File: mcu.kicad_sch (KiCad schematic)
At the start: 46 parts, among them J1 10118193-0001LF, J5 Conn_ARM_SWD_TagConnect_TC2030, SW1 SW_Push, SW2 SW_Push, SW3 SW_Push, U1 RP2040, U2 AP2112K-3.3TRG1, U3 W25Q16JVSSIQ, Y3 12MHZ

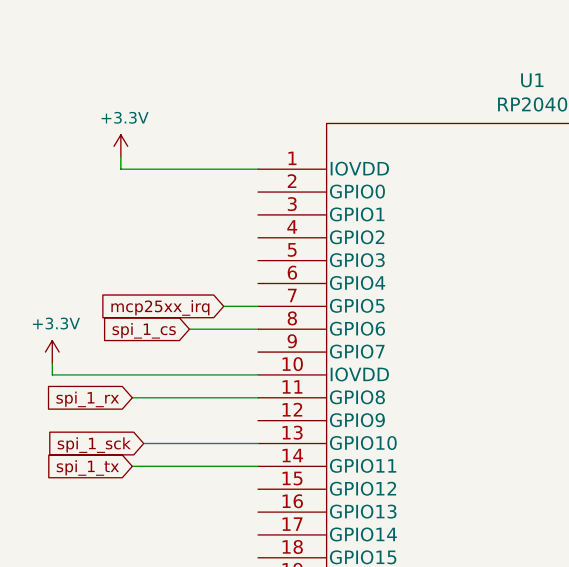
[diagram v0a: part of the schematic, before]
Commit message: move to 4 layers
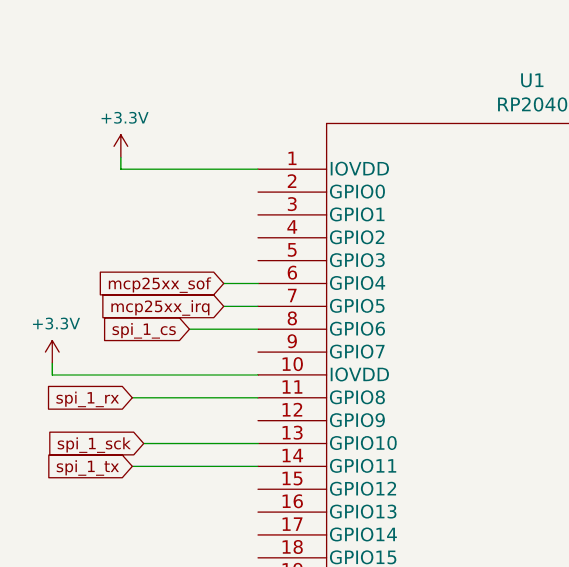
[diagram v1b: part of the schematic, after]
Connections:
- net mcp25xx_sof: now reaches U1.6 (GPIO4)
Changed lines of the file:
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@@
+    (stroke (width 0) (type default))
+  )
+  (wire (pts (xy 35.56 124.46) (xy 39.37 124.46))
     (stroke (width 0) (type default))
   )
@@
       (effects (font (size 1.27 1.27)) hide)
     )
+  )
+  (global_label "mcp25xx_sof" (shape input) (at 35.56 124.46 180)
+    (effects (font (size 1.27 1.27)) (justify right))
+    (property "Intersheetrefs" "${INTERSHEET_REFS}" (at 35.56 124.46 0)
+      (effects (font (size 1.27 1.27)) hide)
+    )

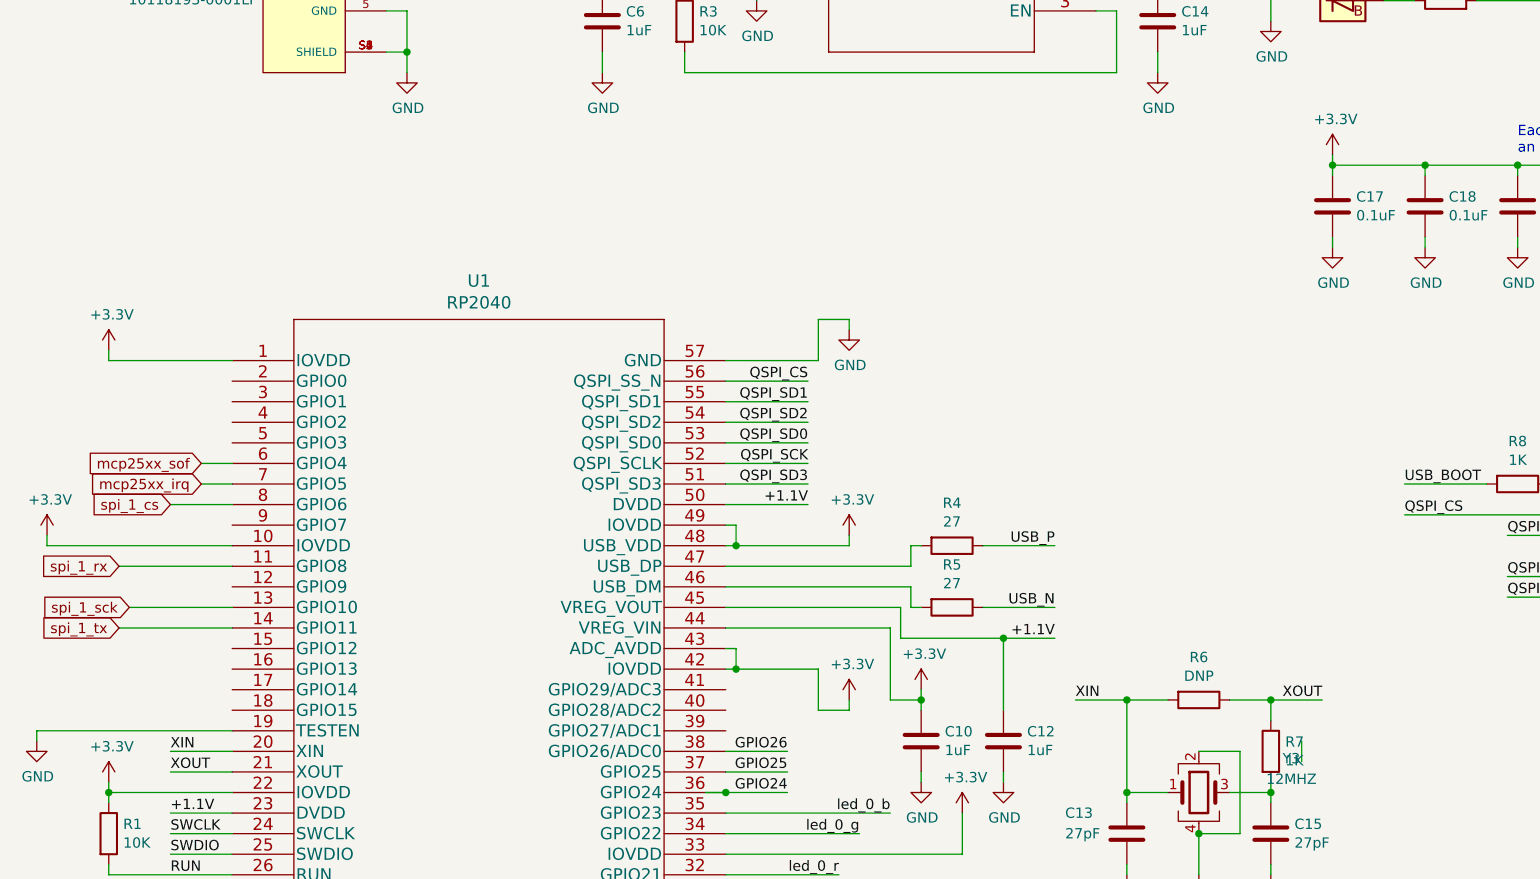
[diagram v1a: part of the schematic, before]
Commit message: Add CAN stby
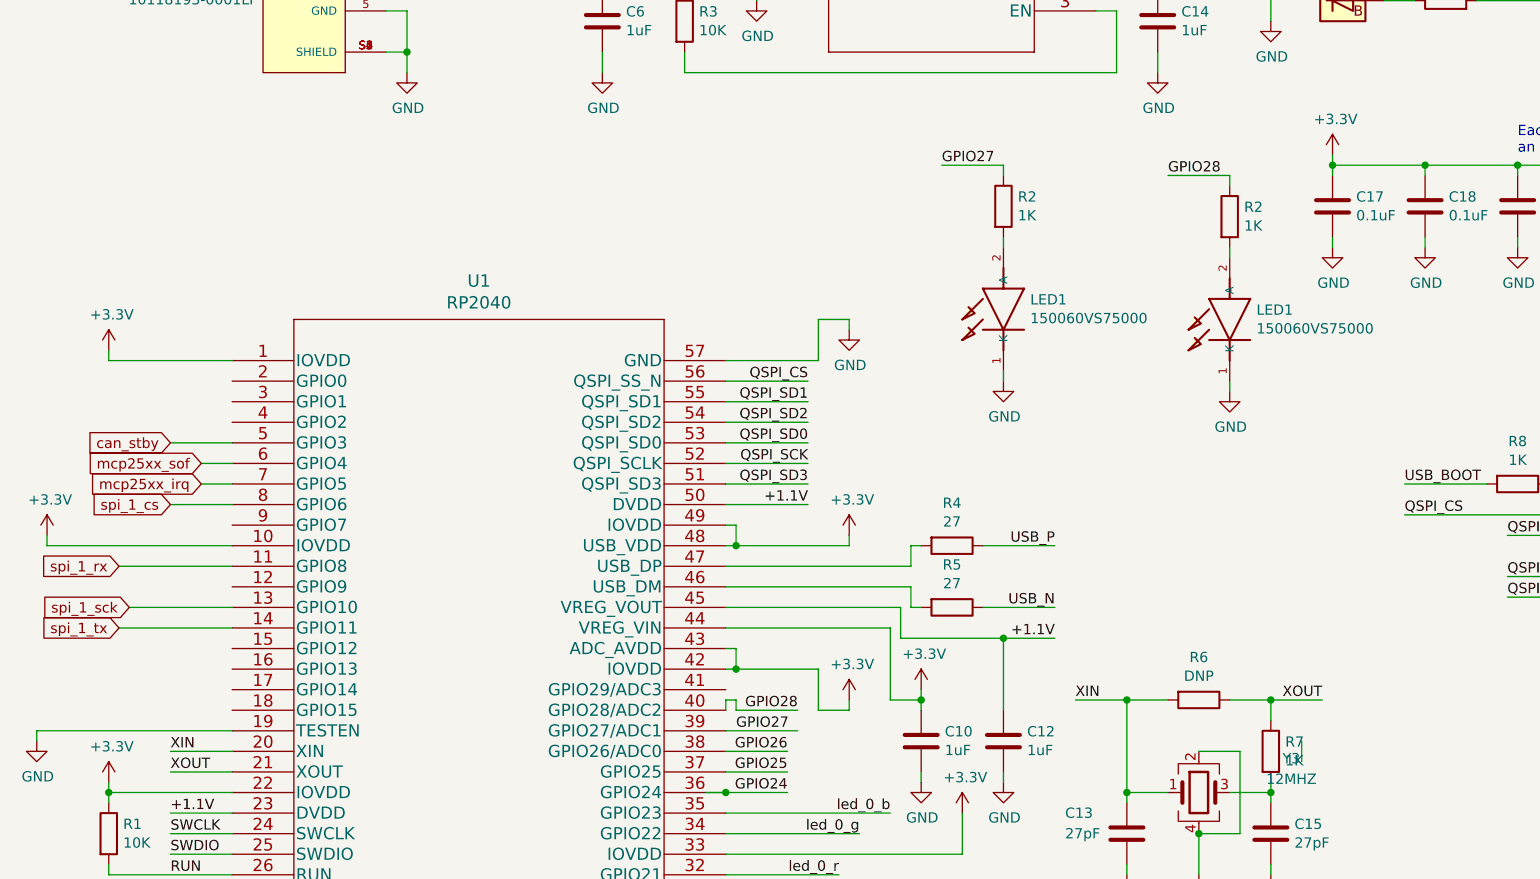
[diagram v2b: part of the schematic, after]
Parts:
- added LED1 (x2): 150060VS75000, LED_SMD:LED_0402_1005Metric, symbol rpi-pico-debugger-shoe-rescue:150060VS75000-150060VS75000
- added R2 (x2): 1K, Resistor_SMD:R_0402_1005Metric, symbol Device:R
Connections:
- net GND: now also LED1.1 (K), LED1.1 (K)
- net GPIO27: now reaches U1.39 (GPIO27/ADC1)
- net GPIO27: now also R2.1
- net GPIO28: now reaches U1.40 (GPIO28/ADC2)
- net GPIO28: now also R2.1
- net can_stby: now reaches U1.5 (GPIO3)
- new net: LED1.2 (A), R2.2 (x2)

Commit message: Verssion 0.11
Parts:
- added C17: 0.1uF, Capacitor_SMD:C_0402_1005Metric, symbol Device:C
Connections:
- net +3V3: now also C17.1
- net GND: now also C17.2
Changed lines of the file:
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@@
   (junction (at 167.64 165.1) (diameter 0) (color 0 0 0 0)
+  )
+  (junction (at 58.42 25.4) (diameter 0) (color 0 0 0 0)
   )
   (junction (at 22.86 25.4) (diameter 0) (color 0 0 0 0)
@@
     (stroke (width 0) (type default))
   )
+  (wire (pts (xy 66.04 25.4) (xy 66.04 36.83))
+    (stroke (width 0) (type default))
+  )
   (wire (pts (xy 26.67 142.24) (xy 39.37 142.24))
     (stroke (width 0) (type default))
@@
     (stroke (width 0) (type default))
   )
+  (wire (pts (xy 66.04 25.4) (xy 58.42 25.4))
+    (stroke (width 0) (type default))
+  )
   (wire (pts (xy 100.33 175.26) (xy 114.3 175.26))
     (stroke (width 0) (type default))
@@
   )
   (wire (pts (xy 149.86 165.1) (xy 149.86 153.67))
+    (stroke (width 0) (type default))
+  )
+  (wire (pts (xy 66.04 44.45) (xy 66.04 45.72))
     (stroke (width 0) (type default))
   )
@@
         (path "/eed35b77-cbf9-4596-9b17-2558f81058ba/643f5372-7b7f-4a0a-9eb8-fe959bdc465c"
           (reference "J5") (unit 1)
+        )
+      )
+    )
+  )
+  (symbol (lib_id "power:GND") (at 66.04 45.72 0) (unit 1)
+    (in_bom yes) (on_board yes) (dnp no)
+    (property "Reference" "#PWR02" (at 66.04 52.07 0)
+      (effects (font (size 1.27 1.27)) hide)
+    )
+    (property "Value" "GND" (at 66.167 50.1142 0)
+      (effects (font (size 1.27 1.27)))
+    )
+    (property "Footprint" "" (at 66.04 45.72 0)
+      (effects (font (size 1.27 1.27)) hide)
+    )
+    (property "Datasheet" "" (at 66.04 45.72 0)
+      (effects (font (size 1.27 1.27)) hide)
+    )
+    (pin "1")
+    (instances
+      (project "rpi-pico-debugger-shoe"
+        (path "/aad74d97-f116-4a83-b498-c8cb2f4b4e35"
+          (reference "#PWR02") (unit 1)
+        )
+      )
+      (project "ltp_kikad"
+        (path "/eed35b77-cbf9-4596-9b17-2558f81058ba/643f5372-7b7f-4a0a-9eb8-fe959bdc465c"
+          (reference "#PWR0116") (unit 1)
         )
       )
@@
         )
       )
+    )
+  )
+  (symbol (lib_id "Device:C") (at 66.04 40.64 0) (unit 1)
+    (in_bom yes) (on_board yes) (dnp no)
+    (property "Reference" "C17" (at 68.961 39.4716 0)
+      (effects (font (size 1.27 1.27)) (justify left))
+    )
+    (property "Value" "0.1uF" (at 68.961 41.783 0)
+      (effects (font (size 1.27 1.27)) (justify left))
+    )
+    (property "Footprint" "Capacitor_SMD:C_0402_1005Metric" (at 67.0052 44.45 0)
+      (effects (font (size 1.27 1.27)) hide)
+    )
+    (property "Datasheet" "~" (at 66.04 40.64 0)
+      (effects (font (size 1.27 1.27)) hide)
+    )
+    (property "Digi-Key_PN" "311-1344-1-ND" (at 66.04 40.64 0)
+      (effects (font (size 1.27 1.27)) hide)
+    )
+    (pin "1")
+    (pin "2")
+    (instances
+      (project "rpi-pico-debugger-shoe"
+        (path "/aad74d97-f116-4a83-b498-c8cb2f4b4e35"
+          (reference "C17") (unit 1)
+        )
+      )
+      (project "ltp_kikad"
+        (path "/eed35b77-cbf9-4596-9b17-2558f81058ba/643f5372-7b7f-4a0a-9eb8-fe959bdc465c"
+          (reference "C39") (unit 1)
+        )
+      )

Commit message: Update crystal footprint, move i2c lines to iner layer
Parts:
- Y3: footprint LTP-305G:ABM3B -> Crystal:Crystal_SMD_3225-4Pin_3.2x2.5mm
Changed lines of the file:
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@@
       (effects (font (size 1.27 1.27)))
     )
-    (property "Footprint" "LTP-305G:ABM3B" (at 158.75 165.1 0)
+    (property "Footprint" "Crystal:Crystal_SMD_3225-4Pin_3.2x2.5mm" (at 158.75 165.1 0)
       (effects (font (size 1.27 1.27)) hide)
     )
